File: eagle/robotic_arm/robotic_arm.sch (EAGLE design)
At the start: 99 parts, among them J2 (ID,OD)=(2.1,5.5)MM, SW1 5A/28V, U6 ATMEGA128RFA1, Y1 16MHz

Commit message: Rev 1: Robotic Arm.  Initial placement of board complete at (3.30x2.50)in or (83.85x63.50)mm.  Might consider putting components on the bottom side of the board
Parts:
- removed C64: 1uF/25V, MrSwirlyEyes:CAP_CERAMIC_SMD-805-1UF-25V-10%
- renumbered FSR1 to FSR_PINKY, FSR2 to FSR_RING, FSR3 to FSR_MIDDLE, FSR4 to FSR_INDEX, FSR5 to FSR_THUMB, S1 to SERVO_PINKY, S2 to SERVO_RING, S3 to SERVO_MIDDLE, S4 to SERVO_INDEX, S5 to SERVO_THUMB, S6 to SERVO_WRIST, TEMP1 to TEMP_PINKY, TEMP2 to TEMP_RING, TEMP3 to TEMP_MIDDLE, TEMP4 to TEMP_INDEX, TEMP5 to TEMP_THUMB, U6 to MCU
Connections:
- removed net 3.3V: C83.1, C94.1, D7.A, VREG1.VOUT
- new net AGND: C18.2, C26.2, C3.2, C4.2, C47.2, C48.2, C49.2, C5.2, C50.2, C51.2, C6.2, C7.2, C85.2, DEMUX1.!EN, DEMUX1.GND, MCU.AVSS, R16.1, R39.1, R40.1, R41.1, R42.1, TEMP_INDEX.GND, TEMP_MIDDLE.GND, TEMP_PINKY.GND, TEMP_RING.GND, TEMP_THUMB.GND, U$2.P$2
- new net AVCC: C18.1, C26.1, C3.1, C4.1, C47.1, C48.1, C49.1, C5.1, C50.1, C51.1, C56.1, C57.1, C6.1, C7.1, C85.1, DEMUX1.VCC, FSR_INDEX.+, FSR_MIDDLE.+, FSR_PINKY.+, FSR_RING.+, FSR_THUMB.+, L1.2, MCU.AREF, MCU.AVDD, MCU.EVDD, TEMP_INDEX.VS, TEMP_MIDDLE.VS, TEMP_PINKY.VS, TEMP_RING.VS, TEMP_THUMB.VS
- net 5V: now also C83.1, C94.1, D7.A, VREG1.VOUT
- net GND: no longer C1.2, C10.2, C11.K, C12.2, C13.K, C14.2, C15.K, C16.2, C17.K, C18.2, C2.K, C26.2, C3.2, C4.2, C47.2, C48.2, C49.2, C5.2, C50.2, C51.2, C6.2, C64.2, C7.2, C8.2, C9.K, DEMUX1.!EN, DEMUX1.GND, MCU.AVSS, R16.1, R39.1, R40.1, R41.1, R42.1, SERVO_INDEX.GND, SERVO_MIDDLE.GND, SERVO_PINKY.GND, SERVO_RING.GND, SERVO_THUMB.GND, SERVO_WRIST.GND, TEMP_INDEX.GND, TEMP_MIDDLE.GND, TEMP_PINKY.GND, TEMP_RING.GND, TEMP_THUMB.GND
- net NGND: now also C1.2, C10.2, C11.K, C12.2, C13.K, C14.2, C15.K, C16.2, C17.K, C2.K, C8.2, C9.K, SERVO_INDEX.GND, SERVO_MIDDLE.GND, SERVO_PINKY.GND, SERVO_RING.GND, SERVO_THUMB.GND, SERVO_WRIST.GND; no longer C85.2, U$2.P$2
- net VCC: no longer C18.1, C26.1, C3.1, C4.1, C47.1, C48.1, C49.1, C5.1, C50.1, C51.1, C56.1, C57.1, C6.1, C64.1, C7.1, C85.1, DEMUX1.VCC, FSR_INDEX.+, FSR_MIDDLE.+, FSR_PINKY.+, FSR_RING.+, FSR_THUMB.+, L1.2, MCU.AREF, MCU.AVDD, MCU.EVDD, TEMP_INDEX.VS, TEMP_MIDDLE.VS, TEMP_PINKY.VS, TEMP_RING.VS, TEMP_THUMB.VS
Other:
- moved on the sheet: C51

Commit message: Rev 1: Robotic Arm.  Initial placement of board with passive components on bottom side of board 3.20x2.50 inches (81.28x63.50mm)
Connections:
- net GND: no longer C83.2, C94.2, C97.2, C98.2, VREG1.GND
- net NGND: now also C83.2, C94.2, C97.2, C98.2, VREG1.GND
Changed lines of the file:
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@@
 <part name="GND125" library="MrSwirlyEyes" deviceset="GND" device=""/>
 <part name="D7" library="MrSwirlyEyes" deviceset="DIODE_GEN-PURP" device="SMD_GP_1A-50V-SOD123F" value="1A/50V"/>
-<part name="GND126" library="MrSwirlyEyes" deviceset="GND" device=""/>
 <part name="C80" library="MrSwirlyEyes" deviceset="CAP_POLARIZED" device="_ALUM-ELECTROLYTIC_SMD_220UF-16V-20%" value="220uF/16V"/>
 <part name="C81" library="MrSwirlyEyes" deviceset="CAP_CERAMIC" device="_SMD-805_0.1UF-50V-10%" value="0.1uF/50V"/>
@@
 <part name="NGND24" library="MrSwirlyEyes" deviceset="AGND" device=""/>
 <part name="SUPPLY50" library="MrSwirlyEyes" deviceset="AVCC" device=""/>
+<part name="NGND27" library="MrSwirlyEyes" deviceset="NGND" device="" value="NGND"/>
 </parts>
 <sheets>
@@
 <instance part="GND125" gate="GND" x="274.32" y="154.94"/>
 <instance part="D7" gate="G$1" x="273.05" y="139.7" rot="R90"/>
-<instance part="GND126" gate="GND" x="274.32" y="109.22"/>
 <instance part="C80" gate="G$1" x="210.82" y="170.18"/>
 <instance part="C81" gate="G$1" x="233.68" y="170.18"/>
@@
 <instance part="NGND24" gate="G$1" x="388.62" y="297.18"/>
 <instance part="SUPPLY50" gate="G$1" x="200.66" y="317.5"/>
+<instance part="NGND27" gate="G$1" x="274.32" y="109.22"/>
 </instances>
 <busses>
@@
 </segment>
 <segment>
-<wire x1="261.62" y1="116.84" x2="261.62" y2="114.3" width="0.1524" layer="91"/>
-<wire x1="261.62" y1="114.3" x2="274.32" y2="114.3" width="0.1524" layer="91"/>
-<wire x1="274.32" y1="114.3" x2="287.02" y2="114.3" width="0.1524" layer="91"/>
-<wire x1="287.02" y1="114.3" x2="287.02" y2="116.84" width="0.1524" layer="91"/>
-<wire x1="274.32" y1="119.38" x2="274.32" y2="114.3" width="0.1524" layer="91"/>
-<junction x="274.32" y="114.3"/>
-<wire x1="274.32" y1="114.3" x2="274.32" y2="111.76" width="0.1524" layer="91"/>
-<pinref part="GND126" gate="GND" pin="GND"/>
-<pinref part="C83" gate="G$1" pin="2"/>
-<pinref part="C94" gate="G$1" pin="2"/>
-<wire x1="294.64" y1="116.84" x2="294.64" y2="114.3" width="0.1524" layer="91"/>
-<wire x1="294.64" y1="114.3" x2="287.02" y2="114.3" width="0.1524" layer="91"/>
-<junction x="287.02" y="114.3"/>
-<pinref part="C98" gate="G$1" pin="2"/>
-<pinref part="C97" gate="G$1" pin="2"/>
-<wire x1="254" y1="116.84" x2="254" y2="114.3" width="0.1524" layer="91"/>
-<wire x1="254" y1="114.3" x2="261.62" y2="114.3" width="0.1524" layer="91"/>
-<junction x="261.62" y="114.3"/>
-<pinref part="VREG1" gate="G$1" pin="GND"/>
-</segment>
-<segment>
 <pinref part="C80" gate="G$1" pin="K"/>
 <wire x1="210.82" y1="165.1" x2="210.82" y2="162.56" width="0.1524" layer="91"/>
@@
 <pinref part="GND21" gate="G$1" pin="NGND"/>
 </segment>
-</net>
+<segment>
+<wire x1="261.62" y1="116.84" x2="261.62" y2="114.3" width="0.1524" layer="91"/>
+<wire x1="261.62" y1="114.3" x2="274.32" y2="114.3" width="0.1524" layer="91"/>
+<wire x1="274.32" y1="114.3" x2="287.02" y2="114.3" width="0.1524" layer="91"/>
+<wire x1="287.02" y1="114.3" x2="287.02" y2="116.84" width="0.1524" layer="91"/>
+<wire x1="274.32" y1="119.38" x2="274.32" y2="114.3" width="0.1524" layer="91"/>
+<junction x="274.32" y="114.3"/>
+<wire x1="274.32" y1="114.3" x2="274.32" y2="111.76" width="0.1524" layer="91"/>
+<pinref part="C83" gate="G$1" pin="2"/>
+<pinref part="C94" gate="G$1" pin="2"/>
+<wire x1="294.64" y1="116.84" x2="294.64" y2="114.3" width="0.1524" layer="91"/>
+<wire x1="294.64" y1="114.3" x2="287.02" y2="114.3" width="0.1524" layer="91"/>
+<junction x="287.02" y="114.3"/>
+<pinref part="C98" gate="G$1" pin="2"/>
+<pinref part="C97" gate="G$1" pin="2"/>
+<wire x1="254" y1="116.84" x2="254" y2="114.3" width="0.1524" layer="91"/>
+<wire x1="254" y1="114.3" x2="261.62" y2="114.3" width="0.1524" layer="91"/>
+<junction x="261.62" y="114.3"/>
+<pinref part="VREG1" gate="G$1" pin="GND"/>
+<pinref part="NGND27" gate="G$1" pin="NGND"/>
+</segment>
+</net>

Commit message: Routed NGND plane + 5V plane + PWM Driver to SERVO sig traces.  Routed TEMP and FSR sig pins to DEMUX.
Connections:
- net SERVO_INDEX: now also SERVO_MIDDLE.SIG; no longer SERVO_INDEX.SIG
- net SERVO_MIDDLE: now also SERVO_INDEX.SIG; no longer SERVO_MIDDLE.SIG
- net SERVO_PINKY: now also SERVO_WRIST.SIG; no longer SERVO_PINKY.SIG
- net SERVO_RING: now also SERVO_THUMB.SIG; no longer SERVO_RING.SIG
- net SERVO_THUMB: now also SERVO_RING.SIG; no longer SERVO_THUMB.SIG
- net SERVO_WRIST: now also SERVO_PINKY.SIG; no longer SERVO_WRIST.SIG
- net TEMP_INDEX: now also TEMP_RING.VOUT; no longer TEMP_INDEX.VOUT
- net TEMP_PINKY: now also TEMP_THUMB.VOUT; no longer TEMP_PINKY.VOUT
- net TEMP_RING: now also TEMP_INDEX.VOUT; no longer TEMP_RING.VOUT
- net TEMP_THUMB: now also TEMP_PINKY.VOUT; no longer TEMP_THUMB.VOUT
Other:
- note added: "WIRE DEMUX"

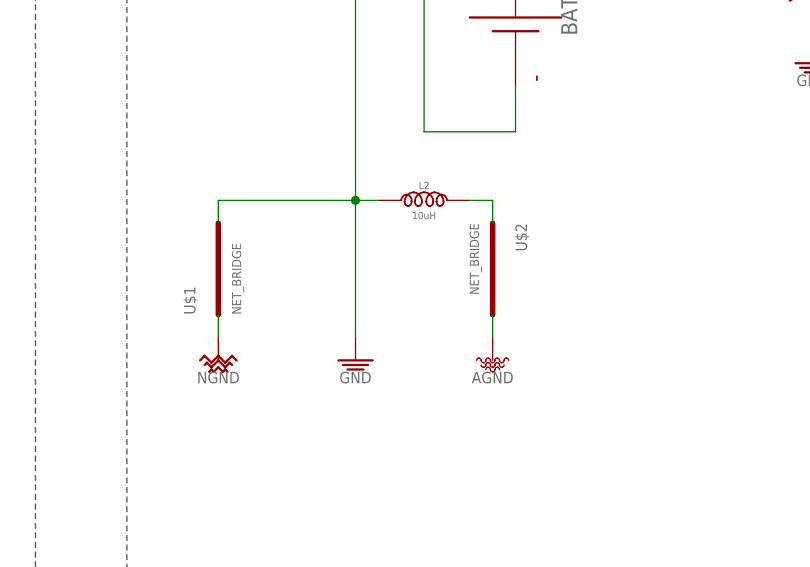
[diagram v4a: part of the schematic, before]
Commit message: Routed AVCC + AGND power planes
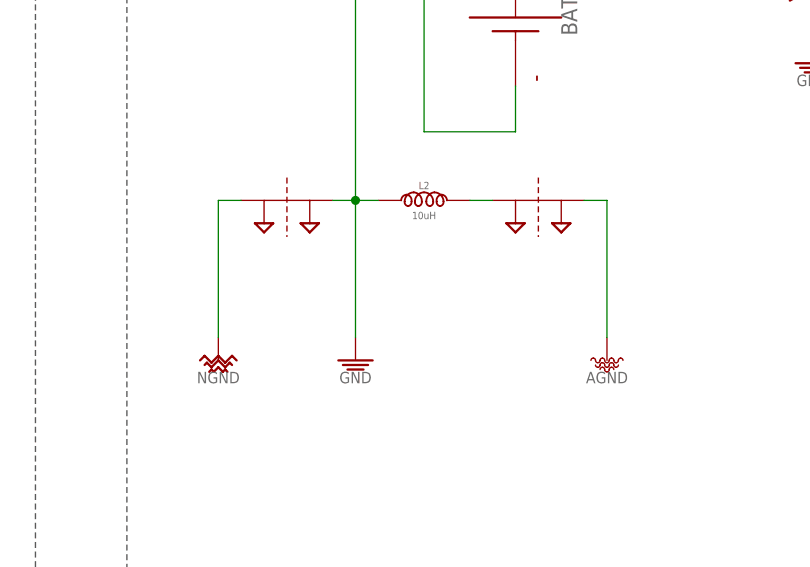
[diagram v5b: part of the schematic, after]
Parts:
- removed U$1, U$2: NET_BRIDGE, MrSwirlyEyes:NET_BRIDGE
- added SUPPLY51, SUPPLY52: 2PT_GND_TIE, SparkFun-PowerSymbols:2PT_GND_TIE
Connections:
- net AGND: now also SUPPLY52.P$2; no longer U$2.P$2
- net GND: now also SUPPLY51.P$2; no longer U$1.P$2
- net N$38: now also SUPPLY52.P$1; no longer U$2.P$1
- net NGND: now also SUPPLY51.P$1; no longer U$1.P$1
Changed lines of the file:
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@@
 <part name="SUPPLY84" library="MrSwirlyEyes" deviceset="VCC" device=""/>
 <part name="BATT1" library="MrSwirlyEyes" deviceset="BATTERY" device="PTH_HOLES"/>
-<part name="U$1" library="MrSwirlyEyes" deviceset="NET_BRIDGE" device=""/>
 <part name="GND124" library="MrSwirlyEyes" deviceset="GND" device=""/>
 <part name="NGND1" library="MrSwirlyEyes" deviceset="NGND" device="" value="NGND"/>
@@
 <part name="GND129" library="MrSwirlyEyes" deviceset="GND" device=""/>
 <part name="SUPPLY85" library="MrSwirlyEyes" deviceset="VCC" device=""/>
-<part name="U$2" library="MrSwirlyEyes" deviceset="NET_BRIDGE" device=""/>
 <part name="L1" library="MrSwirlyEyes" deviceset="INDUCTOR" device="SMD-805_10UH-0.5A-0.65OHM-10%" value="10uH"/>
 <part name="C83" library="MrSwirlyEyes" deviceset="CAP_CERAMIC" device="_SMD-805_0.1UF-50V-10%" value="0.1uF/50V"/>
@@
 <part name="SUPPLY50" library="MrSwirlyEyes" deviceset="AVCC" device=""/>
 <part name="NGND27" library="MrSwirlyEyes" deviceset="NGND" device="" value="NGND"/>
+<part name="SUPPLY51" library="SparkFun-PowerSymbols" deviceset="2PT_GND_TIE" device=""/>
+<part name="SUPPLY52" library="SparkFun-PowerSymbols" deviceset="2PT_GND_TIE" device=""/>
 </parts>
 <sheets>
@@
 <instance part="SUPPLY84" gate="VCC" x="154.94" y="48.26"/>
 <instance part="BATT1" gate="G$1" x="170.18" y="165.1" rot="R270"/>
-<instance part="U$1" gate="G$1" x="137.16" y="137.16" rot="R90"/>
 <instance part="GND124" gate="GND" x="152.4" y="127"/>
 <instance part="NGND1" gate="G$1" x="137.16" y="127"/>
@@
 <instance part="GND129" gate="GND" x="233.68" y="160.02"/>
 <instance part="SUPPLY85" gate="VCC" x="294.64" y="177.8"/>
-<instance part="U$2" gate="G$1" x="167.64" y="137.16" rot="R270"/>
 <instance part="L1" gate="G$1" x="302.26" y="175.26"/>
 <instance part="C83" gate="G$1" x="287.02" y="121.92"/>
@@
 <instance part="SUPPLY47" gate="VCC" x="287.02" y="43.18"/>
 <instance part="SUPPLY48" gate="G$1" x="309.88" y="177.8"/>
-<instance part="NGND2" gate="G$1" x="167.64" y="127"/>
+<instance part="NGND2" gate="G$1" x="180.34" y="127"/>
 <instance part="NGND25" gate="G$1" x="368.3" y="327.66"/>
 <instance part="NGND26" gate="G$1" x="378.46" y="327.66"/>
@@
 <instance part="SUPPLY50" gate="G$1" x="200.66" y="317.5"/>
 <instance part="NGND27" gate="G$1" x="274.32" y="109.22"/>
+<instance part="SUPPLY51" gate="G$1" x="144.78" y="144.78"/>
+<instance part="SUPPLY52" gate="G$1" x="172.72" y="144.78"/>
 </instances>
 <busses>
@@
 <segment>
 <pinref part="GND124" gate="GND" pin="GND"/>
-<pinref part="U$1" gate="G$1" pin="P$2"/>
 <wire x1="152.4" y1="144.78" x2="152.4" y2="129.54" width="0.1524" layer="91"/>
-<wire x1="137.16" y1="142.24" x2="137.16" y2="144.78" width="0.1524" layer="91"/>
-<wire x1="137.16" y1="144.78" x2="152.4" y2="144.78" width="0.1524" layer="91"/>
 <junction x="152.4" y="144.78"/>
 <pinref part="L2" gate="G$1" pin="1"/>
@@
 <wire x1="149.86" y1="167.64" x2="152.4" y2="167.64" width="0.1524" layer="91"/>
 <wire x1="152.4" y1="167.64" x2="152.4" y2="144.78" width="0.1524" layer="91"/>
+<pinref part="SUPPLY51" gate="G$1" pin="P$2"/>
+<wire x1="152.4" y1="144.78" x2="149.86" y2="144.78" width="0.1524" layer="91"/>
 </segment>
 <segment>
@@
 <net name="NGND" class="0">
 <segment>
-<pinref part="U$1" gate="G$1" pin="P$1"/>
-<wire x1="137.16" y1="132.08" x2="137.16" y2="129.54" width="0.1524" layer="91"/>
 <pinref part="NGND1" gate="G$1" pin="NGND"/>
+<wire x1="137.16" y1="129.54" x2="137.16" y2="144.78" width="0.1524" layer="91"/>
+<pinref part="SUPPLY51" gate="G$1" pin="P$1"/>
+<wire x1="137.16" y1="144.78" x2="139.7" y2="144.78" width="0.1524" layer="91"/>
 </segment>
 <segment>
@@
 <pinref part="L2" gate="G$1" pin="2"/>
 <wire x1="165.1" y1="144.78" x2="167.64" y2="144.78" width="0.1524" layer="91"/>
-<pinref part="U$2" gate="G$1" pin="P$1"/>
-<wire x1="167.64" y1="142.24" x2="167.64" y2="144.78" width="0.1524" layer="91"/>
+<pinref part="SUPPLY52" gate="G$1" pin="P$1"/>
 </segment>
 </net>
@@
 </segment>
 <segment>
-<pinref part="U$2" gate="G$1" pin="P$2"/>
-<wire x1="167.64" y1="132.08" x2="167.64" y2="129.54" width="0.1524" layer="91"/>
-<pinref part="NGND2" gate="G$1" pin="AGND"/>
-</segment>
-<segment>
 <pinref part="C18" gate="G$1" pin="2"/>
 <wire x1="368.3" y1="330.2" x2="368.3" y2="332.74" width="0.1524" layer="91"/>
@@
 <pinref part="NGND24" gate="G$1" pin="AGND"/>
 </segment>
-</net>
+<segment>
+<pinref part="SUPPLY52" gate="G$1" pin="P$2"/>
+<wire x1="177.8" y1="144.78" x2="180.34" y2="144.78" width="0.1524" layer="91"/>
+<wire x1="180.34" y1="144.78" x2="180.34" y2="129.54" width="0.1524" layer="91"/>
+<pinref part="NGND2" gate="G$1" pin="AGND"/>
+</segment>
+</net>

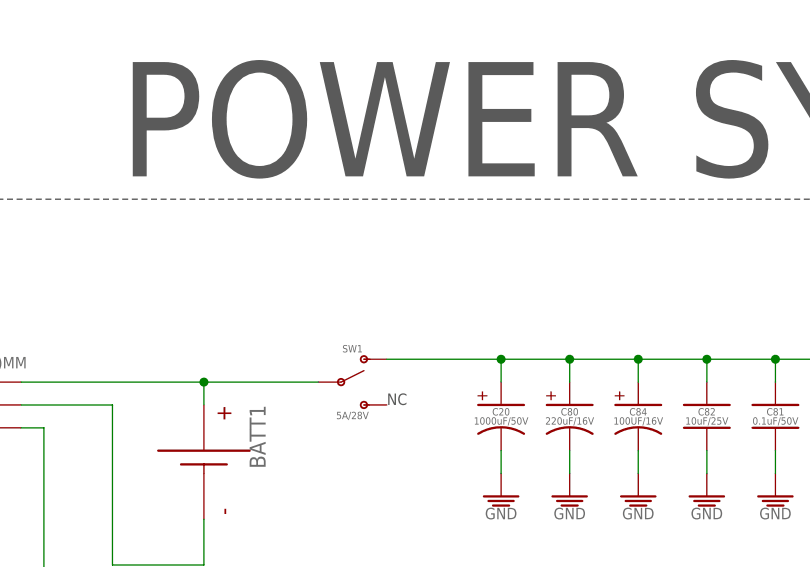
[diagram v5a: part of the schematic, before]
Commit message: Started on immediate power connections
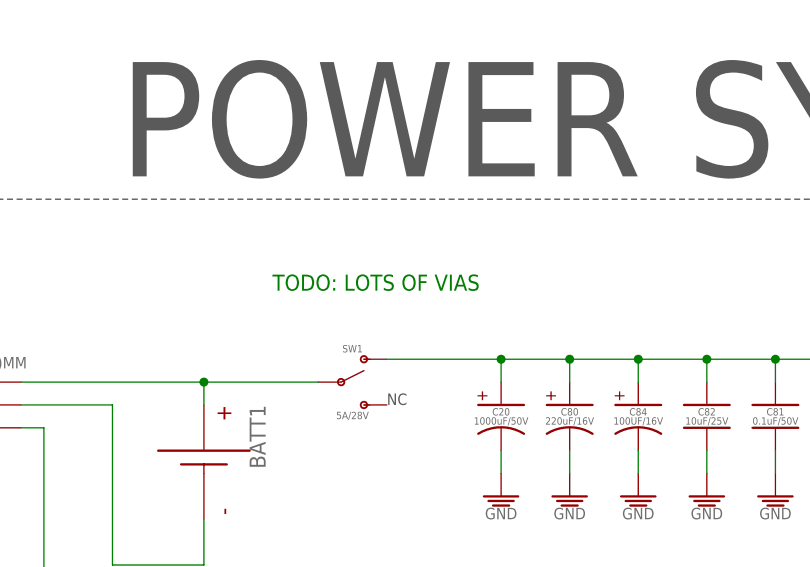
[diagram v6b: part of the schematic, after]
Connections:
- net N$2 renamed BATT_-
- net N$43 renamed BATT_+
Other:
- note added: "TODO: LOTS OF VIAS"
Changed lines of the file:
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@@
 <text x="228.6" y="350.52" size="0.8128" layer="97" font="vector" ratio="20" align="bottom-center">add diode CD1206-S01575</text>
 <text x="287.02" y="269.24" size="1.778" layer="91">WIRE DEMUX</text>
+<text x="177.8" y="182.88" size="1.778" layer="91">TODO: LOTS OF VIAS</text>
 </plain>
 <instances>
@@
 </segment>
 </net>
-<net name="N$43" class="0">
+<net name="BATT_+" class="0">
 <segment>
 <pinref part="BATT1" gate="G$1" pin="P"/>
@@
 </segment>
 </net>
-<net name="N$2" class="0">
+<net name="BATT_-" class="0">
 <segment>
 <pinref part="BATT1" gate="G$1" pin="N"/>
